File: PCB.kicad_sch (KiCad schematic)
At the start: 36 parts, among them J1 Conn_01x04, J2 Screw_Terminal_01x02, J3 Screw_Terminal_01x05, J4 Screw_Terminal_01x05, K1 G5LE-1A_DC3, K2 G5LE-1A_DC3, K3 G5LE-1, K4 G5LE-1, K6 G5LE-1, K7 G5LE-1A_DC3, Q1 DMN65D8L-7, Q2 DMN65D8L-7, Q3 DMN65D8L-7, Q4 DMN65D8L-7, Q5 DMN65D8L-7, Q6 DMN65D8L-7, SW1 Local DI0 (onoff), SW3 Local DI2 (decspeed), SW4 local/remote switch, SW5 Local DI1 (incspeed), U1 WeMos_D1_mini

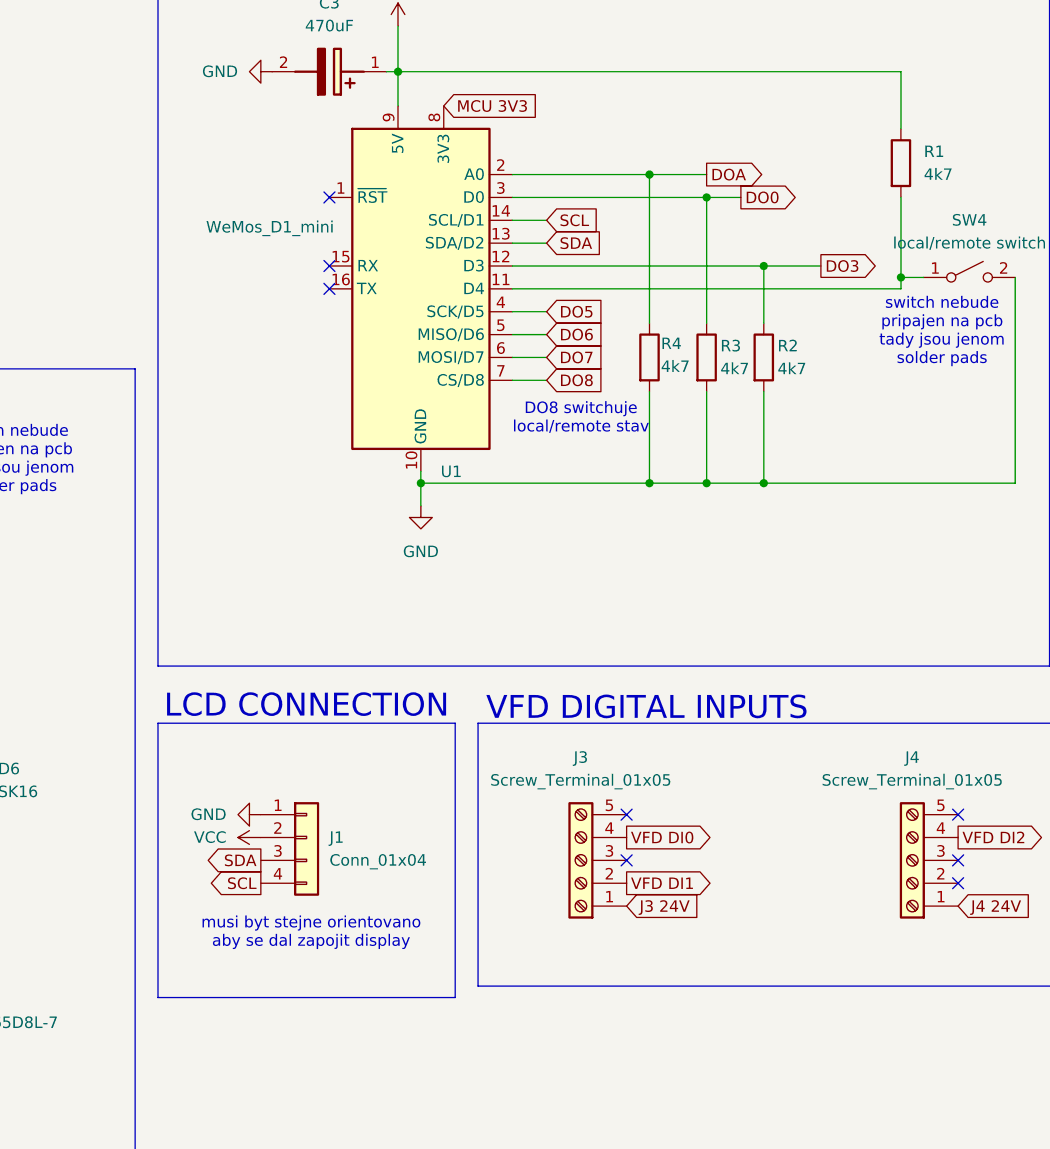
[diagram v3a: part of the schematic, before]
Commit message: aktualizace pcb na zaklade predeslych oprav
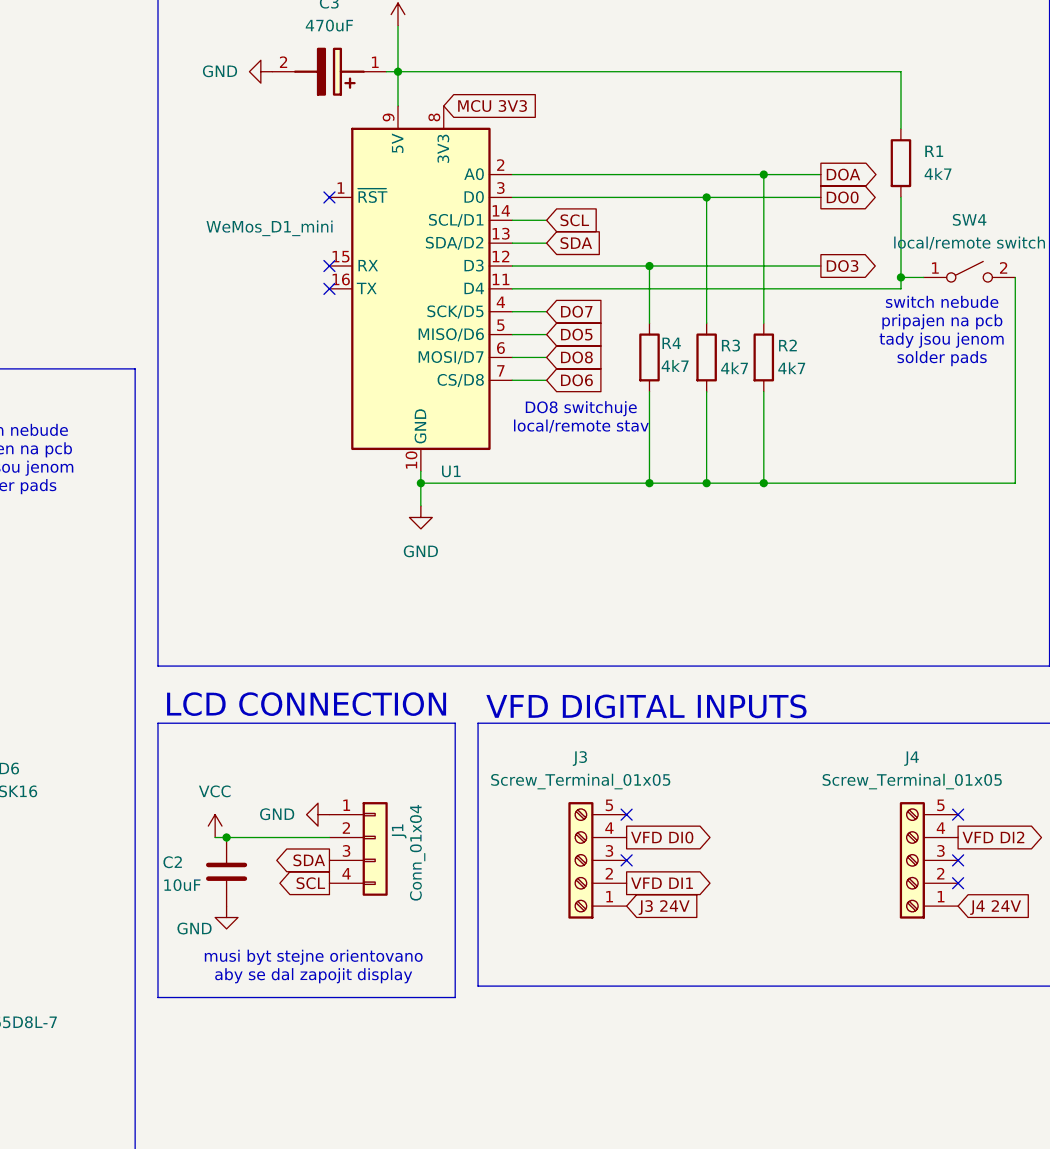
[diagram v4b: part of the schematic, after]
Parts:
- added C2: 10uF, Capacitor_SMD:C_0603_1608Metric, symbol Device:C
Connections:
- net DO3: now also R4.1; no longer R2.1
- net DO5: now also U1.5 (MISO/D6); no longer U1.4 (SCK/D5)
- net DO6: now also U1.7 (CS/D8); no longer U1.5 (MISO/D6)
- net DO7: now also U1.4 (SCK/D5); no longer U1.6 (MOSI/D7)
- net DO8: now also U1.6 (MOSI/D7); no longer U1.7 (CS/D8)
- net DOA: now also R2.1; no longer R4.1
- net GND: now also C2.2
- net VCC: now also C2.1
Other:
- moved on the sheet: J1

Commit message: aktualizace par jmen ve schematu a prave jdu na updatovani pcb
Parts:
- added H1, H10, H11, H2, H4: MountingHole, MountingHole:MountingHole_5mm, symbol Mechanical:MountingHole
- added H3, H5, H6, H8, H9: MountingHole, MountingHole:MountingHole_4mm, symbol Mechanical:MountingHole
- added H7: MountingHole, MountingHole:MountingHole_3mm, symbol Mechanical:MountingHole
- renumbered C1 to C_22uF_1, C3 to C_470uF_3, 1500mA_Fuse1 to Fuse_1500mA_1, J2 to J_24Vin+GND_1, L2 to L_10uH_1, PS1 to PS_DCDC_24V5V_1, R1 to R_4k7_1, R4 to R_4k7_2, R3 to R_4k7_3, R2 to R_4k7_4, SW4 to SW_LocRem_1
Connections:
- net DO5: now also Q6.1 (G), U1.4 (SCK/D5); no longer Q4.1 (G), U1.5 (MISO/D6)
- net DO6: now also Q4.1 (G), U1.5 (MISO/D6); no longer Q5.1 (G), U1.7 (CS/D8)
- net DO7: now also Q1.1 (G), Q2.1 (G), Q3.1 (G), U1.6 (MOSI/D7); no longer Q6.1 (G), U1.4 (SCK/D5)
- net DO8: now also Q5.1 (G), U1.7 (CS/D8); no longer Q1.1 (G), Q2.1 (G), Q3.1 (G), U1.6 (MOSI/D7)
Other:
- note added: "DO7 switchuje local/remote stav"
- note added: "MOUNTING HOLES"
- note removed: "DO8 switchuje local/remote stav"
- moved on the sheet: R_4k7_2, R_4k7_3, R_4k7_4

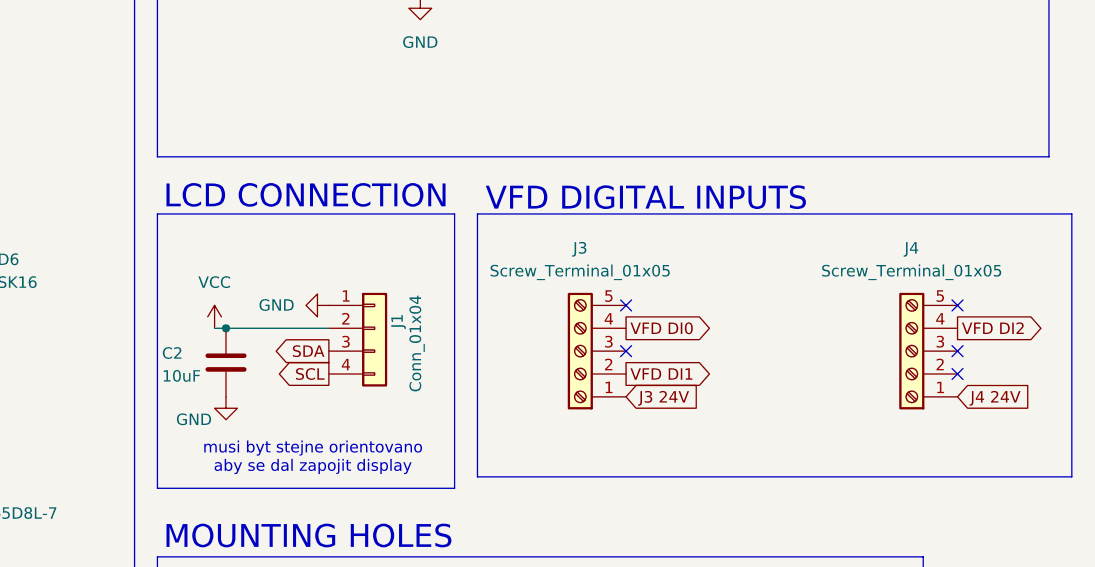
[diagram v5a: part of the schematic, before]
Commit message: change the names of the schematic
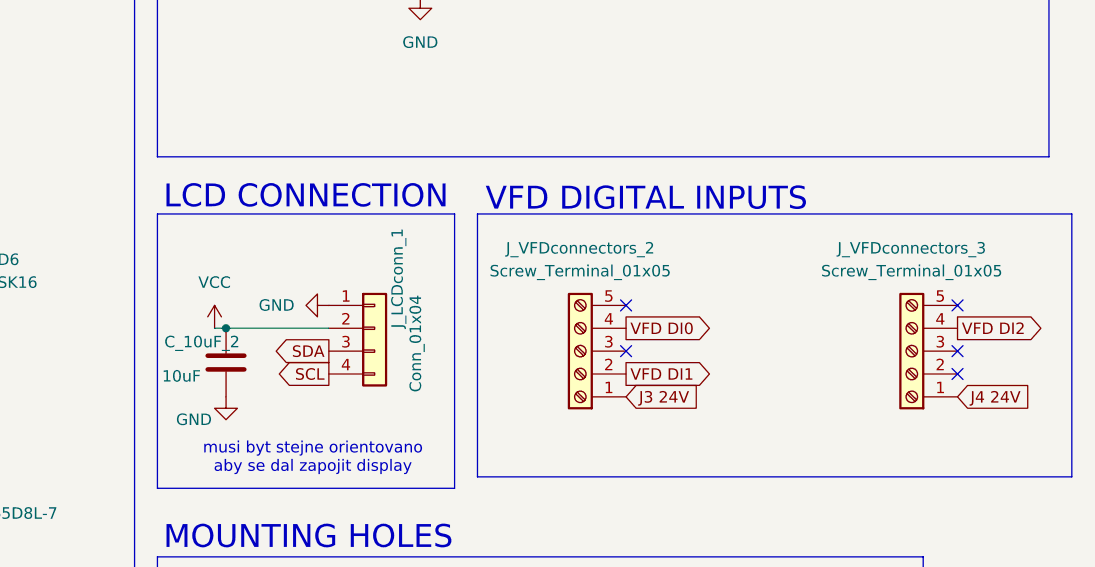
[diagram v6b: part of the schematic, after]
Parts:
- renumbered C2 to C_10uF_2, J1 to J_LCDconn_1, J3 to J_VFDconnectors_2, J4 to J_VFDconnectors_3
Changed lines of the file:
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@@
 		(dnp no)
 		(fields_autoplaced yes)
-		(property "Reference" "J3"
+		(property "Reference" "J_VFDconnectors_2"
 			(at 229.87 111.76 0)
 			(effects
@@
 			(project ""
 				(path "/a03e0b08-fd2d-4304-b838-c1c22de42e47"
-					(reference "J3")
+					(reference "J_VFDconnectors_2")
 					(unit 1)
 				)
@@
 		(on_board yes)
 		(dnp no)
-		(property "Reference" "C2"
-			(at 183.388 123.444 0)
+		(property "Reference" "C_10uF_2"
+			(at 183.642 122.174 0)
 			(effects
 				(font
@@
 			(project "PCB"
 				(path "/a03e0b08-fd2d-4304-b838-c1c22de42e47"
-					(reference "C2")
+					(reference "C_10uF_2")
 					(unit 1)
 				)
@@
 		(on_board yes)
 		(dnp no)
-		(property "Reference" "J1"
+		(property "Reference" "J_LCDconn_1"
 			(at 209.55 120.6499 90)
 			(effects
@@
 			(project ""
 				(path "/a03e0b08-fd2d-4304-b838-c1c22de42e47"
-					(reference "J1")
+					(reference "J_LCDconn_1")
 					(unit 1)
 				)
@@
 		(dnp no)
 		(fields_autoplaced yes)
-		(property "Reference" "J4"
+		(property "Reference" "J_VFDconnectors_3"
 			(at 266.7 111.76 0)
 			(effects
@@
 			(project "PCB"
 				(path "/a03e0b08-fd2d-4304-b838-c1c22de42e47"
-					(reference "J4")
+					(reference "J_VFDconnectors_3")
 					(unit 1)
 				)
